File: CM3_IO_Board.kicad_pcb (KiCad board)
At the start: 2 copper layers, 93.3 x 116.8 mm, 54 parts, among them J1 Bus_PCI_Express_Mini, J11 USB_A, J2 USB_B_Micro, J3 Conn_02x03_Odd_Even, J4 Conn_02x09_Odd_Even, J5 Conn_01x02, J6 Conn_01x02, J7 Screw_Terminal_01x02, J8 Micro_SD_Card, J9 Conn_01x02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

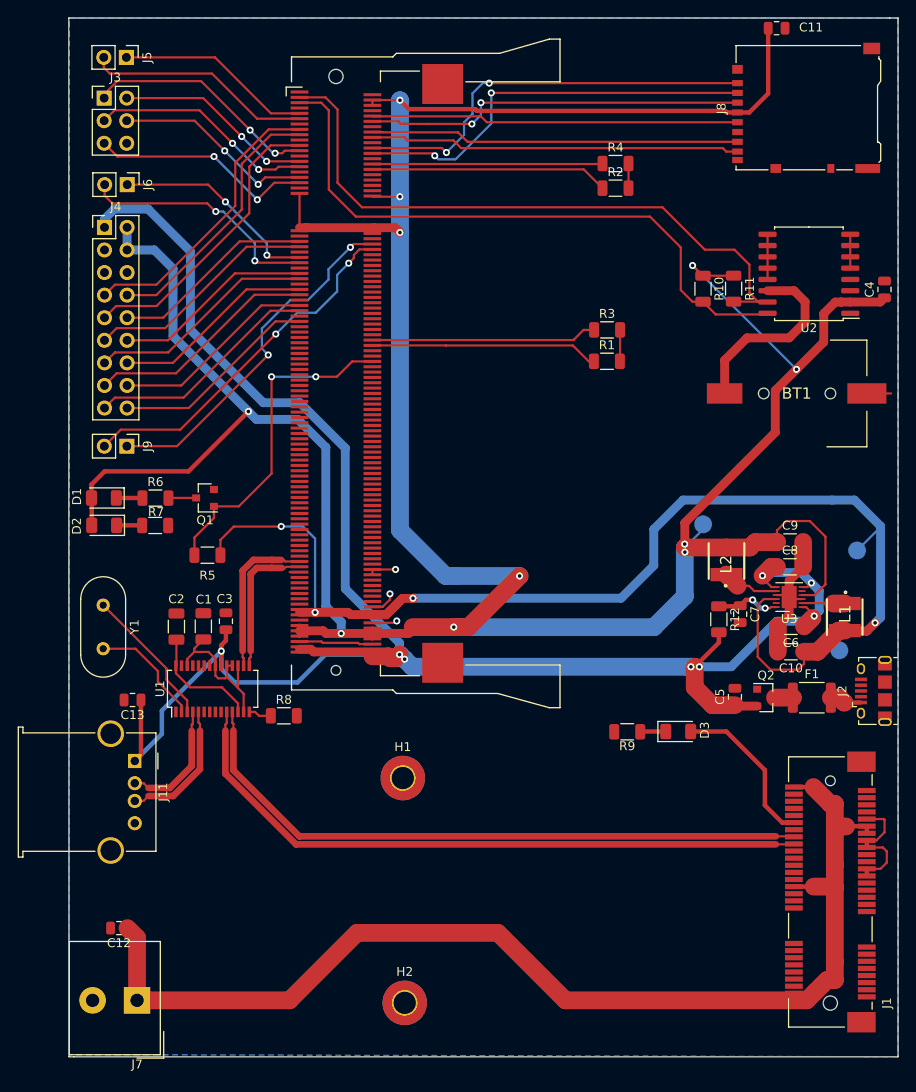
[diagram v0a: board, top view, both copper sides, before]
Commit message: 5V connection point increased
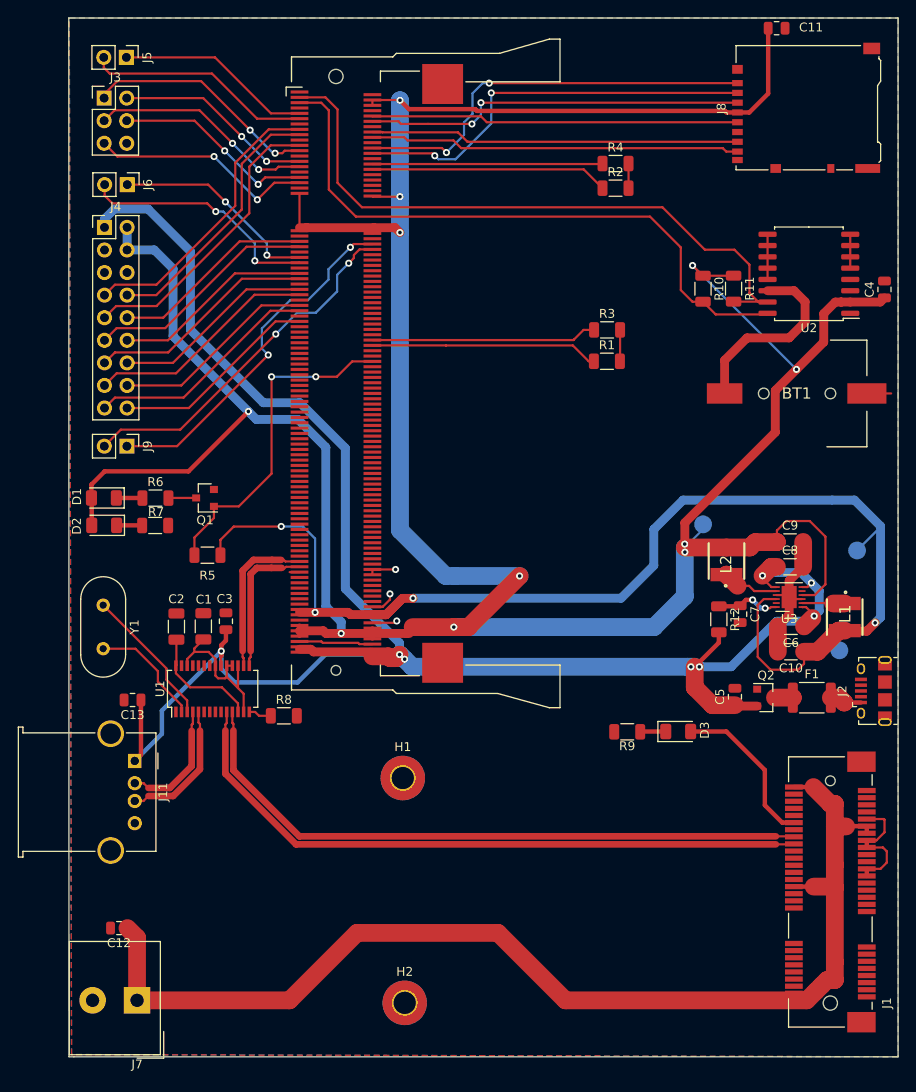
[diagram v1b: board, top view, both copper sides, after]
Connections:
- J4 pad 3: GND -> +5V
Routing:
- added copper zone on F.Cu, net GND
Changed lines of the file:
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@@
   )
   (setup
-    (last_trace_width 2)
+    (last_trace_width 1)
     (user_trace_width 0.5)
     (user_trace_width 1)
@@
       (net 6 +3V3))
     (pad 3 thru_hole oval (at 0 2.54) (size 1.7 1.7) (drill 1) (layers *.Cu *.Mask)
-      (net 1 GND))
+      (net 5 +5V))
     (pad 4 thru_hole oval (at 2.54 2.54) (size 1.7 1.7) (drill 1) (layers *.Cu *.Mask)
       (net 6 +3V3))
@@
       (effects (font (size 1 1) (thickness 0.15)))
     )
+    (fp_circle (center 0 0) (end 2.5 0) (layer Cmts.User) (width 0.15))
+    (fp_circle (center 0 0) (end 2.75 0) (layer F.CrtYd) (width 0.05))
     (fp_text user %R (at 0.3 0) (layer F.Fab)
       (effects (font (size 1 1) (thickness 0.15)))
     )
-    (fp_circle (center 0 0) (end 2.5 0) (layer Cmts.User) (width 0.15))
-    (fp_circle (center 0 0) (end 2.75 0) (layer F.CrtYd) (width 0.05))
     (pad 1 connect circle (at 0 0) (size 5 5) (layers B.Cu B.Mask)
       (net 1 GND))
@@
       (effects (font (size 1 1) (thickness 0.15)))
     )
+    (fp_circle (center 0 0) (end 2.5 0) (layer Cmts.User) (width 0.15))
+    (fp_circle (center 0 0) (end 2.75 0) (layer F.CrtYd) (width 0.05))
     (fp_text user %R (at 0.3 0) (layer F.Fab)
       (effects (font (size 1 1) (thickness 0.15)))
     )
-    (fp_circle (center 0 0) (end 2.5 0) (layer Cmts.User) (width 0.15))
-    (fp_circle (center 0 0) (end 2.75 0) (layer F.CrtYd) (width 0.05))
     (pad 1 connect circle (at 0 0) (size 5 5) (layers B.Cu B.Mask)
       (net 1 GND))
@@
   (segment (start 71.67 64.9) (end 74.07 62.5) (width 0.25) (layer B.Cu) (net 191))
   (segment (start 69.57 64.9) (end 71.67 64.9) (width 0.25) (layer B.Cu) (net 191))
+  (zone (net 1) (net_name GND) (layer F.Cu) (hatch none 0.508)
+    (connect_pads (clearance 0.245))
+    (min_thickness 0.254)
+    (fill yes (arc_segments 32) (thermal_gap 0.508) (thermal_bridge_width 0.508))
+    (polygon
+      (pts
+        (xy 137.16 148.59) (xy 44.196 148.336) (xy 43.942 31.75) (xy 137.16 31.75)
+      )
+    )
+  )
   (zone (net 1) (net_name GND) (layer B.Cu) (hatch none 0.508)
     (connect_pads (clearance 0.245))
@@
     (polygon
       (pts
-        (xy 137.16 148.59) (xy 43.942 148.336) (xy 43.942 31.75) (xy 137.16 31.75)
+        (xy 137.16 148.59) (xy 44.196 148.336) (xy 43.942 31.75) (xy 137.16 31.75)
       )
     )

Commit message: logo added
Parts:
- added G***: LOGO, graphics:Front layer logo, F.Cu at (103.4, 86.9)
- added G***: LOGO, graphics:Front layer logo, B.Cu at (93.5, 77.2)
- renumbered D1 to ACT, D3 to INT, D2 to PWR
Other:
- board text added: "+3.3V"
- board text added: "1"
- board text added: "12"
- board text added: "12MHz"
- board text added: "13"
- board text added: "16"
- board text added: "17"
- board text added: "18"
- board text added: "19"
- board text added: "1:SPI0_CE1_N"
- board text added: "2"
- board text added: "20"
- board text added: "21"
- board text added: "22"
- board text added: "2:SPI0_CE0_N"
- board text added: "3"
- board text added: "3.3V"
- board text added: "3:SPI0_MISO"
- board text added: "4"
- board text added: "4:SPI0_MOSI"
- board text added: "5"
- board text added: "5:SPI0_SCLK"
- board text added: "5V"
- board text added: "6"
- board text added: "6:N/A"
- board text added: "DESIGNED BY"
- board text added: "GND"
- board text added: "J3 PINOUT"
- board text added: "LTE MODULE"
- board text added: "RXD0"
- board text added: "RXD1"
- board text added: "SCL"
- board text added: "SDA"
- board text added: "TXD0"
- board text added: "TXD1"
